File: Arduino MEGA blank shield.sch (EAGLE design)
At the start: 14 parts

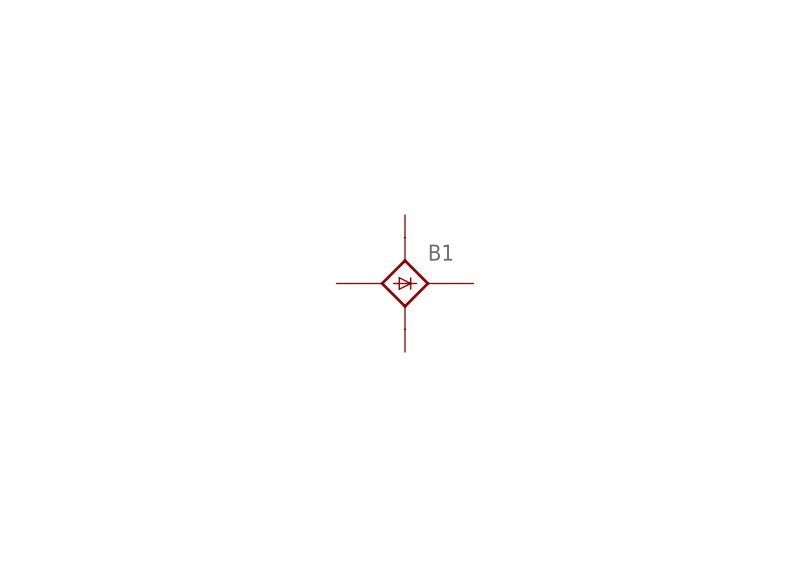
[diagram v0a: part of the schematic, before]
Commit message: removed dummy part
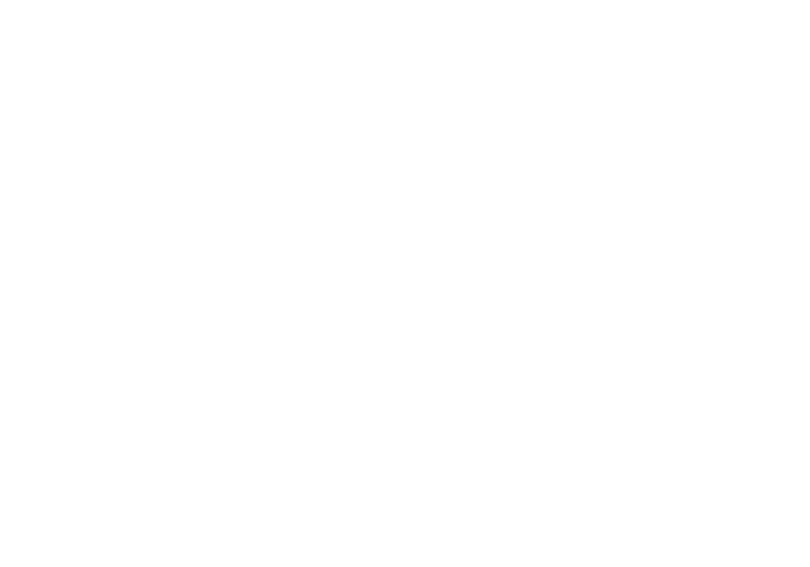
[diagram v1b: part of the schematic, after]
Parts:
- removed B1: (no value), rectifier:B25A-
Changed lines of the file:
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@@
 <part name="JP5" library="pinhead" deviceset="PINHD-1X1" device=""/>
 <part name="JP6" library="pinhead" deviceset="PINHD-1X1" device=""/>
-<part name="B1" library="rectifier" deviceset="B25A-" device=""/>
 </parts>
 <sheets>
@@
 <attribute name="VALUE" x="331.47" y="119.38" size="1.778" layer="96"/>
 </instance>
-<instance part="B1" gate="G$1" x="104.14" y="132.08"/>
 </instances>
 <busses>

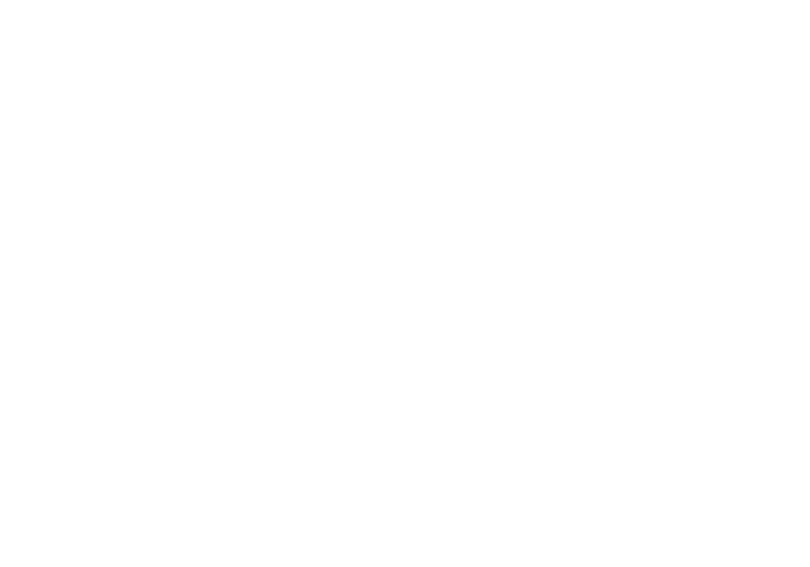
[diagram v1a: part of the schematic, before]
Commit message: real addition of header
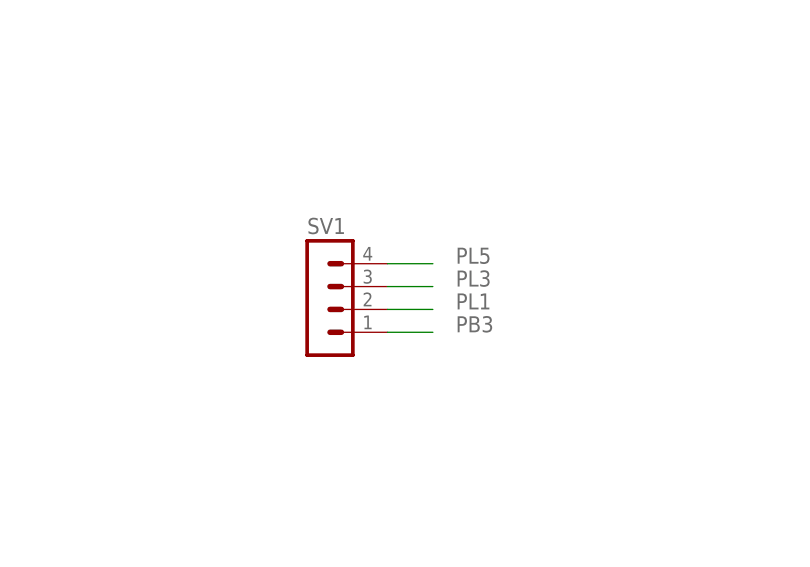
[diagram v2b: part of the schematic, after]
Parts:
- added SV1: (no value), con-lstb:MA04-1
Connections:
- net PB3: now also SV1.1
- net PL1: now also SV1.2
- net PL3: now also SV1.3
- net PL5: now also SV1.4
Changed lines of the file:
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@@
 <part name="JP5" library="pinhead" deviceset="PINHD-1X1" device=""/>
 <part name="JP6" library="pinhead" deviceset="PINHD-1X1" device=""/>
+<part name="SV1" library="con-lstb" deviceset="MA04-1" device=""/>
 </parts>
 <sheets>
@@
 <attribute name="VALUE" x="331.47" y="119.38" size="1.778" layer="96"/>
 </instance>
+<instance part="SV1" gate="1" x="91.44" y="127"/>
 </instances>
 <busses>
@@
 <label x="62.23" y="71.755" size="1.778" layer="95"/>
 <pinref part="JP2" gate="A" pin="4"/>
+</segment>
+<segment>
+<pinref part="SV1" gate="1" pin="1"/>
+<wire x1="104.14" y1="121.92" x2="99.06" y2="121.92" width="0.1524" layer="91"/>
+<label x="106.68" y="121.92" size="1.778" layer="95"/>
 </segment>
 </net>
@@
 <pinref part="JP2" gate="A" pin="6"/>
 </segment>
+<segment>
+<pinref part="SV1" gate="1" pin="2"/>
+<wire x1="104.14" y1="124.46" x2="99.06" y2="124.46" width="0.1524" layer="91"/>
+<label x="106.68" y="124.46" size="1.778" layer="95"/>
+</segment>
 </net>
 <net name="PL2" class="0">
@@
 <pinref part="JP2" gate="A" pin="8"/>
 </segment>
+<segment>
+<pinref part="SV1" gate="1" pin="3"/>
+<wire x1="104.14" y1="127" x2="99.06" y2="127" width="0.1524" layer="91"/>
+<label x="106.68" y="127" size="1.778" layer="95"/>
+</segment>
 </net>
 <net name="PL4" class="0">
@@
 <pinref part="JP2" gate="A" pin="10"/>
 </segment>
-</net>
+<segment>
+<pinref part="SV1" gate="1" pin="4"/>
+<wire x1="104.14" y1="129.54" x2="99.06" y2="129.54" width="0.1524" layer="91"/>
+<label x="106.68" y="129.54" size="1.778" layer="95"/>
+</segment>
+</net>

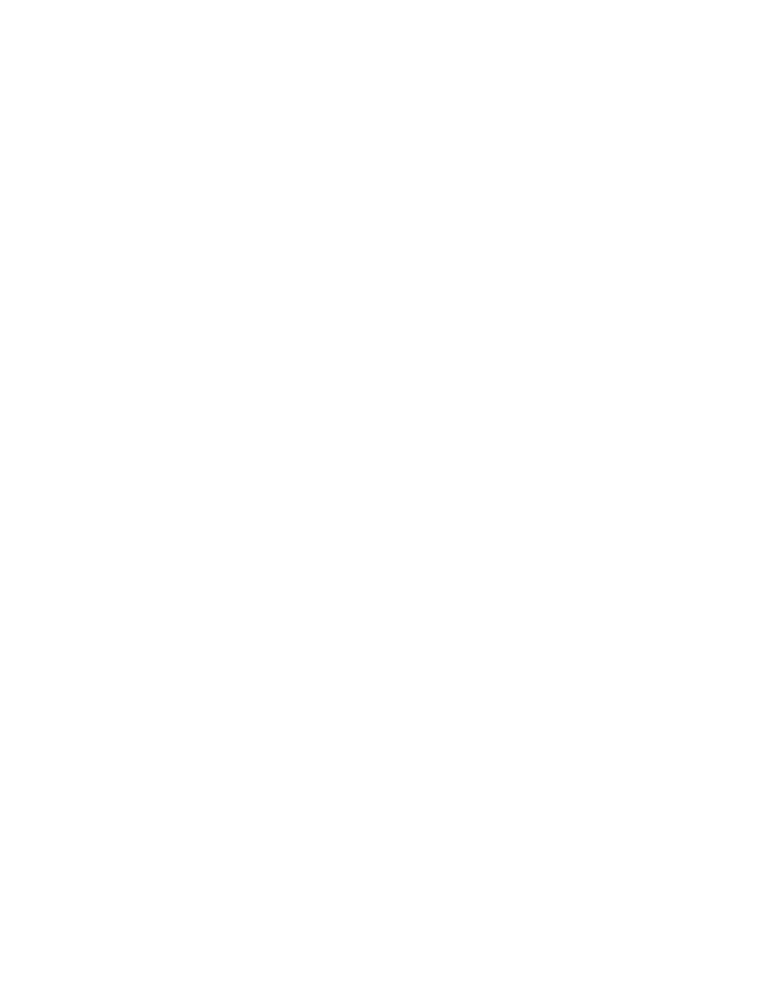
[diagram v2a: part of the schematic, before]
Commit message: added motor controls
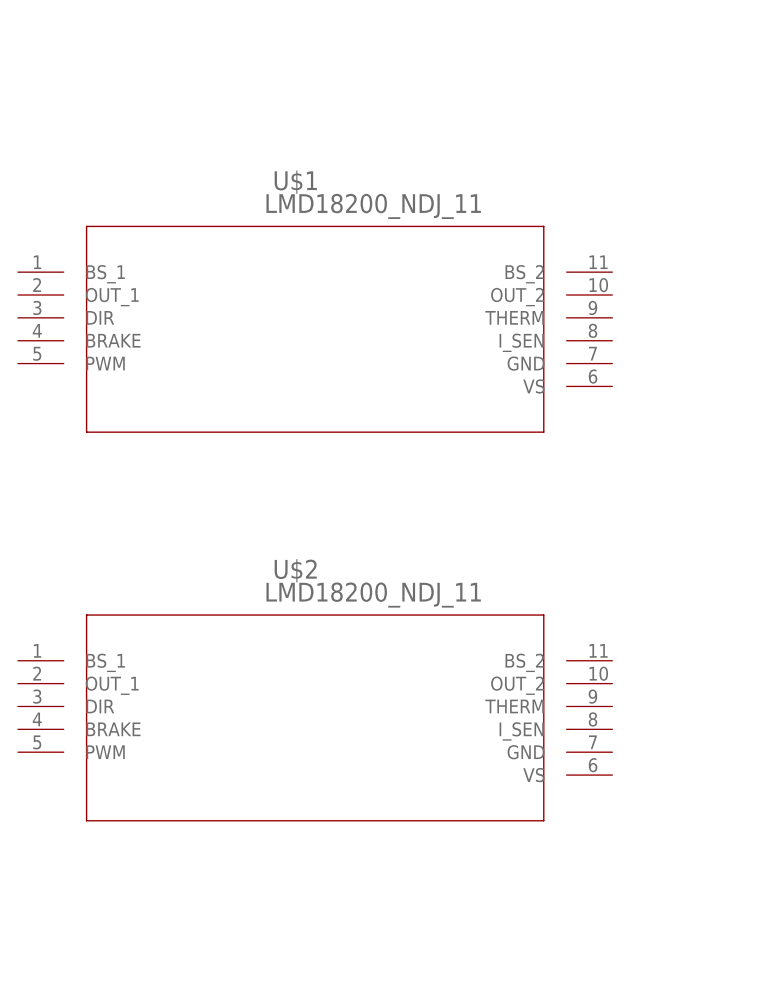
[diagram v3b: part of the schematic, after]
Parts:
- added U$1, U$2: LMD18200_NDJ_11, mega2560shield:LMD18200_NDJ_11
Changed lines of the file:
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@@
 <part name="JP6" library="pinhead" deviceset="PINHD-1X1" device=""/>
 <part name="SV1" library="con-lstb" deviceset="MA04-1" device=""/>
+<part name="U$1" library="mega2560shield" deviceset="LMD18200_NDJ_11" device=""/>
+<part name="U$2" library="mega2560shield" deviceset="LMD18200_NDJ_11" device=""/>
 </parts>
 <sheets>
@@
 </instance>
 <instance part="SV1" gate="1" x="91.44" y="127"/>
+<instance part="U$1" gate="A" x="-10.16" y="167.64"/>
+<instance part="U$2" gate="A" x="-10.16" y="124.46"/>
 </instances>
 <busses>

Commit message: headers added and LMD18200t circuit added
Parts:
- removed U$2: LMD18200_NDJ_11, mega2560shield:LMD18200_NDJ_11
- added CAPACITOR_330UF, CAPACITOR_330UF1: C1206, Brians_Library:C1206
- added RESISTOR-12K, RESISTOR-12K1: R1206, Brians_Library:R1206
- added SV2, SV3, SV4, SV5, SV6, SV7, SV8, SV9: (no value), con-lstb:MA04-1
- added U$3: LMD18200_NDJ_11, IEEELMD18200t:LMD18200_NDJ_11
- U$1: device mega2560shield:LMD18200_NDJ_11 -> IEEELMD18200t:LMD18200_NDJ_11
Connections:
- new net 12V: RESISTOR-12K.1, RESISTOR-12K1.1
- new net EXTRA: SV9.2
- new net EXTRA2: SV9.1
- new net MOTOR_OUT1: U$3.OUT_1
- new net MOTOR_OUT2: U$3.OUT_2
- new net M_OUT1: U$1.OUT_1
- new net M_OUT2: U$1.OUT_2
- new net N$1: U$1.DIR
- new net N$6: U$3.DIR
- new net R2_OUT: RESISTOR-12K1.2, U$1.PWM
- new net R_OUT: RESISTOR-12K.2, U$3.PWM
- new net VIN2: CAPACITOR_330UF1.1, U$1.VS
- net GND: now also CAPACITOR_330UF.2, CAPACITOR_330UF1.2, U$1.GND, U$3.GND
- net PA0: now also SV9.4
- net PA1: now also SV9.3
- net PA2: now also SV6.4
- net PA3: now also SV6.3
- net PA4: now also SV2.4
- net PA5: now also SV6.2
- net PA6: now also SV2.2
- net PA7: now also SV6.1
- net PB2: now also SV4.1
- net PB5: now also SV8.1
- net PB6: now also SV8.2
- net PB7: now also SV8.3
- net PC0: now also SV5.2
- net PC1: now also SV3.2
- net PC2: now also SV5.3
- net PC3: now also SV3.3
- net PC4: now also SV5.4
- net PC5: now also SV3.4
- net PC6: now also SV7.3
- net PC7: now also SV7.4
- net PD7: now also SV3.1
- net PE4: now also SV8.4
- net PE5: now also SV2.3
- net PG0: now also SV7.1
- net PG2: now also SV5.1
- net PG5: now also SV2.1
- net PL0: now also SV4.2
- net PL2: now also SV4.3
- net PL4: now also SV4.4
- net PL7: now also SV7.2
- net VIN: now also CAPACITOR_330UF.1, U$3.VS
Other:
- moved on the sheet: U$1
